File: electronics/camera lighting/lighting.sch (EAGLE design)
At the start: 10 parts

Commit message: pre-production PCBs
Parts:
- removed P1: (no value), jst-ph:JST-PH2
- added PWR: (no value), jst-ph:JST-PH2
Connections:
- net 5V: now also PWR.2; no longer P1.1
- net GND: now also PWR.1; no longer P1.2
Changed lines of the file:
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@@
 <part name="D7" library="adafruit" deviceset="LED" device="CHIPLED_1206"/>
 <part name="D8" library="adafruit" deviceset="LED" device="CHIPLED_1206"/>
-<part name="P1" library="jst-ph" deviceset="JST-PH2" device=""/>
+<part name="PWR" library="jst-ph" deviceset="JST-PH2" device=""/>
 </parts>
 <sheets>
@@
 <instance part="D7" gate="G$1" x="86.36" y="45.72"/>
 <instance part="D8" gate="G$1" x="96.52" y="45.72"/>
-<instance part="P1" gate="G$1" x="12.7" y="55.88"/>
+<instance part="PWR" gate="G$1" x="12.7" y="53.34" rot="MR180"/>
 </instances>
 <busses>
@@
 <wire x1="60.96" y1="60.96" x2="60.96" y2="63.5" width="0.1524" layer="91"/>
 <label x="58.42" y="63.5" size="1.778" layer="95"/>
-<pinref part="P1" gate="G$1" pin="1"/>
-<wire x1="20.32" y1="55.88" x2="20.32" y2="60.96" width="0.1524" layer="91"/>
 <wire x1="20.32" y1="60.96" x2="60.96" y2="60.96" width="0.1524" layer="91"/>
 <junction x="60.96" y="60.96"/>
+<pinref part="PWR" gate="G$1" pin="2"/>
+<wire x1="20.32" y1="55.88" x2="20.32" y2="60.96" width="0.1524" layer="91"/>
 </segment>
 </net>
@@
 <wire x1="60.96" y1="40.64" x2="60.96" y2="38.1" width="0.1524" layer="91"/>
 <junction x="60.96" y="40.64"/>
-<pinref part="P1" gate="G$1" pin="2"/>
-<wire x1="20.32" y1="53.34" x2="20.32" y2="40.64" width="0.1524" layer="91"/>
 <wire x1="20.32" y1="40.64" x2="25.4" y2="40.64" width="0.1524" layer="91"/>
 <junction x="25.4" y="40.64"/>
+<pinref part="PWR" gate="G$1" pin="1"/>
+<wire x1="20.32" y1="53.34" x2="20.32" y2="40.64" width="0.1524" layer="91"/>
 </segment>
 </net>

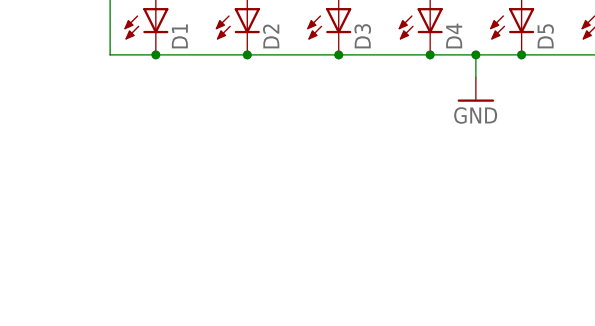
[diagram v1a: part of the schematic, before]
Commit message: updated all PCBs and added PDF schematics
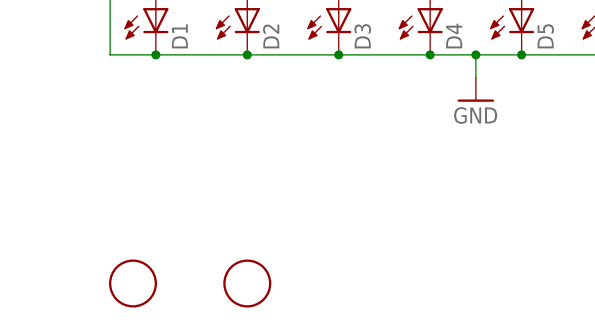
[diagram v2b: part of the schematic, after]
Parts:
- added U$1, U$2: FIDUCIAL, adafruit:FIDUCIAL
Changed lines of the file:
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@@
 <part name="D8" library="adafruit" deviceset="LED" device="CHIPLED_1206"/>
 <part name="PWR" library="jst-ph" deviceset="JST-PH2" device=""/>
+<part name="U$1" library="adafruit" deviceset="FIDUCIAL" device=""/>
+<part name="U$2" library="adafruit" deviceset="FIDUCIAL" device=""/>
 </parts>
 <sheets>
@@
 <instance part="D8" gate="G$1" x="96.52" y="45.72"/>
 <instance part="PWR" gate="G$1" x="12.7" y="53.34" rot="MR180"/>
+<instance part="U$1" gate="G$1" x="22.86" y="15.24"/>
+<instance part="U$2" gate="G$1" x="35.56" y="15.24"/>
 </instances>
 <busses>
